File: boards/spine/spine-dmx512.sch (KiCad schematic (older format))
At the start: 22 parts, among them P2 XLR_3, Q1 IRFML8244, Q2 IRFML8244, U3 NC7WZ14, U4 NC7WZ14, U5 NC7WZ14, U6 SN75176B, X1 100BASET_XFMR

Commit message: Tidy
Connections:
- wire segments 110 -> 106
- no-connect marks 5 -> 9
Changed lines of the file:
@@
 Text Label 1950 1950 0    60   ~ 0
 DMX_TX_OOK
-Text Label 8900 4500 0    60   ~ 0
+Text Label 8950 4500 0    60   ~ 0
 DMX_PWR1
-Text Label 8900 4900 0    60   ~ 0
+Text Label 8950 4900 0    60   ~ 0
 DMX_PWR2
-Text Label 8900 5500 0    60   ~ 0
+Text Label 8950 5500 0    60   ~ 0
 DMX_TX_OOK
-Text Label 8900 5900 0    60   ~ 0
+Text Label 8950 5900 0    60   ~ 0
 DMX_GND
 Text Notes 900  1350 0    60   ~ 0
@@
 Connection ~ 2950 1350
 Wire Wire Line
-	8700 4900 9550 4900
+	8700 4900 9600 4900
 Wire Wire Line
 	2600 1950 1950 1950
@@
 	2600 1050 1950 1050
 Wire Wire Line
-	8700 4500 9550 4500
-Wire Wire Line
-	8700 5500 9550 5500
-Wire Wire Line
-	8700 4700 8800 4700
-Wire Wire Line
-	8700 5900 8800 5900
-Wire Wire Line
-	8800 5900 9550 5900
-Connection ~ 8800 5900
-Wire Wire Line
-	8800 4700 8800 5900
+	8700 4500 9600 4500
+Wire Wire Line
+	8700 5500 9600 5500
+Wire Wire Line
+	8700 4700 8850 4700
+Wire Wire Line
+	8700 5900 8850 5900
+Wire Wire Line
+	8850 5900 9600 5900
+Connection ~ 8850 5900
+Wire Wire Line
+	8850 4700 8850 5900
 Wire Wire Line
 	5500 5900 6950 5900
@@
 	2600 6350 3850 6350
 Wire Wire Line
-	4200 6350 4800 6350
-Wire Wire Line
-	4800 6350 5400 6350
-Wire Wire Line
-	5400 6350 5950 6350
+	3850 6350 4800 6350
+Wire Wire Line
+	4800 6350 5950 6350
 Wire Wire Line
 	5950 6350 6400 6350
@@
 	3150 4050 3850 4050
 Wire Wire Line
-	3850 4050 4200 4050
-Wire Wire Line
-	4200 4050 4800 4050
-Wire Wire Line
-	4800 4050 5400 4050
-Wire Wire Line
-	5400 4050 6800 4050
+	3850 4050 4800 4050
+Wire Wire Line
+	4800 4050 6800 4050
 Connection ~ 6800 4700
 Wire Wire Line
@@
 Connection ~ 3850 4050
 Wire Wire Line
-	3850 4900 3850 6350
+	3850 6350 3850 4900
 Connection ~ 2850 4050
 Connection ~ 3850 6350
@@
 Text Notes 6900 6200 0    60   ~ 0
 DC blocking
-Wire Wire Line
-	3850 6350 4200 6350
+NoConn ~ 4050 4950
+NoConn ~ 4050 5350
+NoConn ~ 5000 5700
+NoConn ~ 5000 6100
 $EndSCHEMATC

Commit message: Get the BOM started
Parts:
- removed unit 1 of U4
- added unit 1 of U5
- C1, C2, C7: value .1uF -> 0.1uF; MfgId (none) -> CC0805ZRY5V9BB104; MfrId (none) -> Yageo; RefPrice1k (none) -> 0.00783; Vend1 (none) -> Digikey; Vend1Id (none) -> 311-1361-1-ND
- C3, C6: MfgId (none) -> CC0805ZKY5V6BB106; MfrId CC0805ZKY5V6BB106 -> Yageo; RefPrice1k (none) -> 0.03080; Vend1 (none) -> Digikey; Vend1Id (none) -> 311-1355-1-ND
- C4, C5: MfgId (none) -> CC0805KRX7R9BB102; MfrId (none) -> Yageo; RefPrice1k (none) -> 0.00981; Vend1 (none) -> Digikey; Vend1Id (none) -> 311-1127-1-ND
- D1, D2: value D_Schottky_x2_KCom_AAK -> BAT54 2x common cathode; MfrId (none) -> Diodes Inc; RefPrice1k (none) -> .03955; Vend1 (none) -> Digikey; Vend1Id (none) -> BAT54C-FDICT-ND
- D3: value 20V -> TVS 20V Zener; MfgId (none) -> MMBZ20VALT1G; MfrId MMBZ20VALT1G -> ON Semi; RefPrice1k (none) -> .04208; Vend1 (none) -> Digikey; Vend1Id (none) -> MMBZ20VALT1GOSCT-ND
- P2: value XLR_3 -> XLR-3 Female; MfgId (none) -> NC3FAAH2-0; MfrId (none) -> Neutrik; RefPrice1k (none) -> 0.653; Vend1 (none) -> Mouser; Vend1Id (none) -> 568-NC3FAAH-2-O
- Q1, Q2: MfgId (none) -> IRFML8244TRPBF; MfrId (none) -> Infineon; RefPrice1k (none) -> 0.1046; Vend1 (none) -> Digikey; Vend1Id (none) -> IRFML8244TRPBFCT-ND
- R1, R2: MfgId (none) -> RMCF0805JT4K70; MfrId (none) -> Stackpole; RefPrice1k (none) -> 0.0032; Vend1 (none) -> Digikey; Vend1Id (none) -> RMCF0805JT4K70CT-ND
- R3: MfgId (none) -> RMCF0805JT150R; MfrId (none) -> Stackpole; RefPrice1k (none) -> 0.0032; Vend1 (none) -> Digikey; Vend1Id (none) -> RMCF0805JT150RCT-ND
- R4: MfgId (none) -> RMCF0805JT1M00; MfrId (none) -> Stackpole; RefPrice1k (none) -> 0.0032; Vend1 (none) -> Digikey; Vend1Id (none) -> RMCF0805JT1M00CT-ND
- T1: renamed from X1; value 100BASET_XFMR -> 10/100baseT transformer; footprint xess-J00-0045 -> (none); MfgId (none) -> PT61018PEL; MfrId (none) -> Bourns; RefPrice1k (none) -> 0.78; Vend1 (none) -> Mouser; Vend1Id (none) -> 652-PT61018PEL
- U3, U4, U5: MfgId (none) -> NC7WZ14P6X; MfrId (none) -> Fairchild; RefPrice1k (none) -> 0.07631; Vend1 (none) -> Digikey; Vend1Id (none) -> NC7WZ14P6XCT-ND
- U4: renamed from U5; MfgId (none) -> NC7WZ14P6X; MfrId (none) -> Fairchild; RefPrice1k (none) -> 0.07631; Vend1 (none) -> Digikey; Vend1Id (none) -> NC7WZ14P6XCT-ND
- U6: MfgId (none) -> SN75176BDR; MfrId (none) -> Texas Instruments; RefPrice1k (none) -> 0.330; Vend1 (none) -> Digikey; Vend1Id (none) -> 296-1275-1-ND
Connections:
- wire segments 106 -> 81

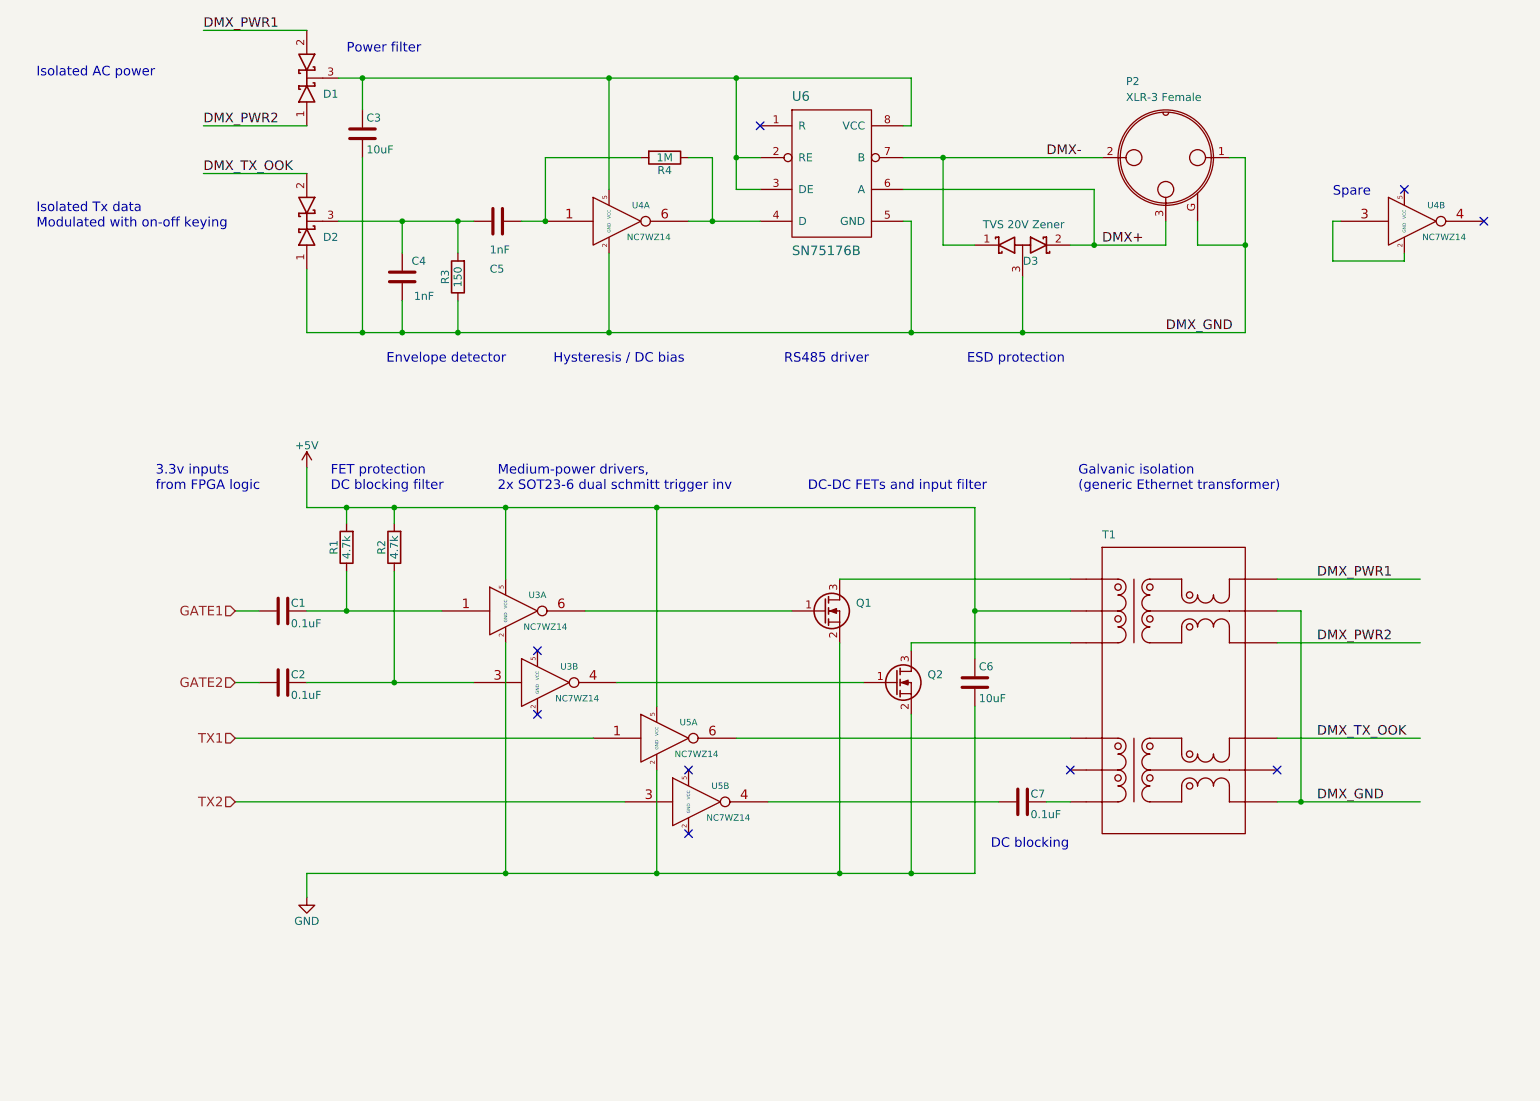
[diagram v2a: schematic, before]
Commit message: USB port: ESD, crystal, eeprom
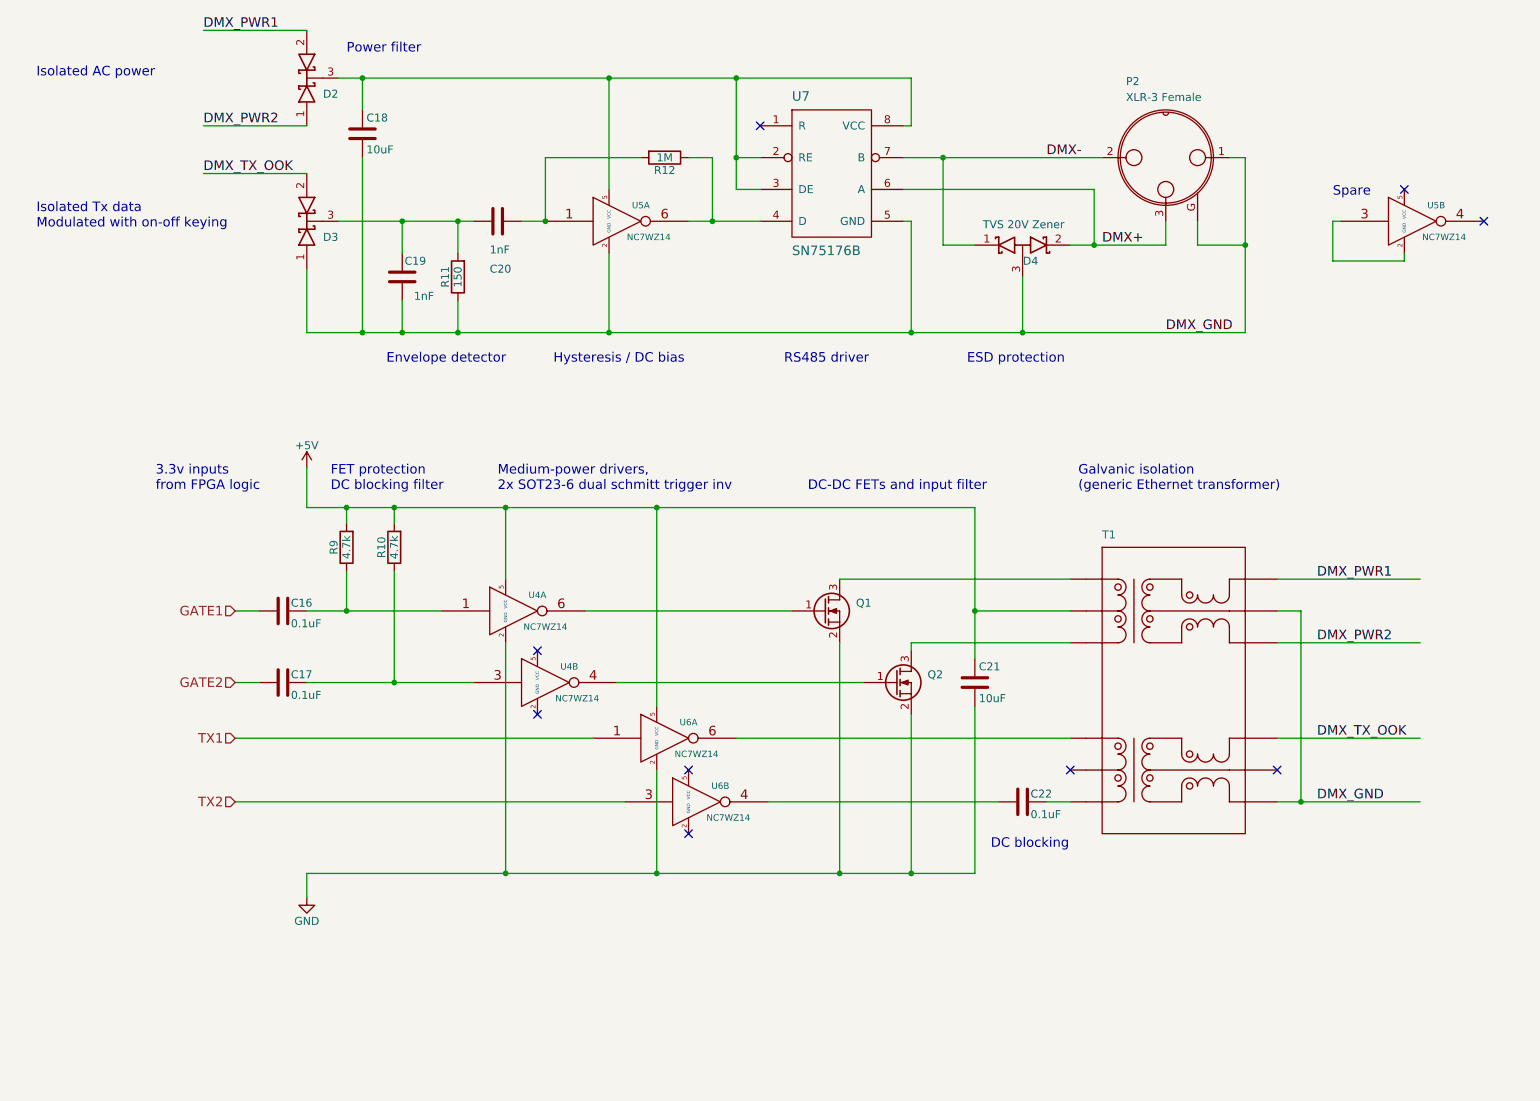
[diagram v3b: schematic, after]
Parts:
- renumbered C1 to C16, C2 to C17, C3 to C18, C4 to C19, C5 to C20, C6 to C21, C7 to C22, D1 to D2, D2 to D3, D3 to D4, R2 to R10, R3 to R11, R4 to R12, R1 to R9, U3 to U4, U4 to U5, U5 to U6, U6 to U7
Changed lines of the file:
@@
 DMX-
 $Comp
-L SN75176B U6
+L SN75176B U7
 U 1 1 563E894A
 P 5950 1550
-F 0 "U6" H 5650 1600 60  0000 L BNN
+F 0 "U7" H 5650 1600 60  0000 L BNN
 F 1 "SN75176B" H 5650 700 60  0000 L TNN
 F 2 "" H 5950 1550 60  0000 C CNN
@@
 $EndComp
 $Comp
-L D_Schottky_x2_ACom_KKA D3
+L D_Schottky_x2_ACom_KKA D4
 U 1 1 563E8FC2
 P 7100 2400
-F 0 "D3" H 7150 2300 50  0000 C CNN
+F 0 "D4" H 7150 2300 50  0000 C CNN
 F 1 "TVS 20V Zener" H 6850 2500 50  0000 L BNN
 F 2 "" H 7100 2400 60  0000 C CNN
@@
 $EndComp
 $Comp
-L NC7WZ14 U4
+L NC7WZ14 U5
 U 1 1 563ECD2E
 P 4550 2250
-F 0 "U4" H 4700 2350 40  0000 C CNN
+F 0 "U5" H 4700 2350 40  0000 C CNN
 F 1 "NC7WZ14" H 4750 2150 40  0000 C CNN
 F 2 "" H 4550 2250 60  0000 C CNN
@@
 NoConn ~ 9500 2050
 $Comp
-L R R4
+L R R12
 U 1 1 563ED073
 P 4850 1850
-F 0 "R4" V 4930 1850 50  0000 C CNN
+F 0 "R12" V 4930 1850 50  0000 C CNN
 F 1 "1M" V 4850 1850 50  0000 C CNN
 F 2 "" V 4780 1850 30  0000 C CNN
@@
 NoConn ~ 10000 2250
 $Comp
-L C C4
+L C C19
 U 1 1 563EDC1A
 P 3200 2600
-F 0 "C4" H 3050 2700 50  0000 L CNN
+F 0 "C19" H 3050 2700 50  0000 L CNN
 F 1 "1nF" H 3000 2450 50  0000 L BNN
 F 2 "" H 3238 2450 30  0000 C CNN
@@
 $EndComp
 $Comp
-L D_Schottky_x2_KCom_AAK D2
+L D_Schottky_x2_KCom_AAK D3
 U 1 1 563EE535
 P 2600 2250
-F 0 "D2" V 2500 2100 50  0000 C CNN
+F 0 "D3" V 2500 2100 50  0000 C CNN
 F 1 "BAT54 2x common cathode" H 2600 2350 50  0001 C CNN
 F 2 "" H 2600 2250 60  0000 C CNN
@@
 NoConn ~ 7400 5700
 $Comp
-L C C6
+L C C21
 U 1 1 563F0E74
 P 6800 5150
-F 0 "C6" H 6825 5250 50  0000 L CNN
+F 0 "C21" H 6825 5250 50  0000 L CNN
 F 1 "10uF " H 6825 5050 50  0000 L CNN
 F 2 "" H 6838 5000 30  0000 C CNN
@@
 $EndComp
 $Comp
-L GND #PWR02
+L GND #PWR18
 U 1 1 563F2AEF
 P 2600 6500
-F 0 "#PWR02" H 2600 6250 50  0001 C CNN
+F 0 "#PWR18" H 2600 6250 50  0001 C CNN
 F 1 "GND" H 2600 6350 50  0000 C CNN
 F 2 "" H 2600 6500 60  0000 C CNN
@@
 $EndComp
 $Comp
-L C C1
+L C C16
 U 1 1 563F4706
 P 2450 4700
-F 0 "C1" V 2400 4750 50  0000 L CNN
+F 0 "C16" V 2400 4750 50  0000 L CNN
 F 1 "0.1uF" V 2500 4750 50  0000 L TNN
 F 2 "" H 2488 4550 30  0000 C CNN
@@
 $EndComp
 $Comp
-L +5V #PWR03
+L +5V #PWR17
 U 1 1 563F515D
 P 2600 3800
-F 0 "#PWR03" H 2600 3650 50  0001 C CNN
+F 0 "#PWR17" H 2600 3650 50  0001 C CNN
 F 1 "+5V" H 2600 3940 50  0000 C CNN
 F 2 "" H 2600 3800 60  0000 C CNN
@@
 NoConn ~ 5000 6100
 $Comp
-L D_Schottky_x2_KCom_AAK D1
+L D_Schottky_x2_KCom_AAK D2
 U 1 1 563ED560
 P 2600 1350
-F 0 "D1" V 2500 1200 50  0000 C CNN
+F 0 "D2" V 2500 1200 50  0000 C CNN
 F 1 "BAT54 2x common cathode" H 2600 1450 50  0001 C CNN
 F 2 "" H 2600 1350 60  0000 C CNN
@@
 $EndComp
 $Comp
-L C C3
+L C C18
 U 1 1 563F1736
 P 2950 1700
-F 0 "C3" H 2975 1800 50  0000 L CNN
+F 0 "C18" H 2975 1800 50  0000 L CNN
 F 1 "10uF " H 2975 1600 50  0000 L CNN
 F 2 "" H 2988 1550 30  0000 C CNN
@@
 $EndComp
 $Comp
-L NC7WZ14 U4
+L NC7WZ14 U5
 U 2 1 563F235B
 P 9550 2250
-F 0 "U4" H 9700 2350 40  0000 C CNN
+F 0 "U5" H 9700 2350 40  0000 C CNN
 F 1 "NC7WZ14" H 9750 2150 40  0000 C CNN
 F 2 "" H 9550 2250 60  0000 C CNN
@@
 $EndComp
 $Comp
-L NC7WZ14 U3
+L NC7WZ14 U4
 U 1 1 563F23E5
 P 3900 4700
-F 0 "U3" H 4050 4800 40  0000 C CNN
+F 0 "U4" H 4050 4800 40  0000 C CNN
 F 1 "NC7WZ14" H 4100 4600 40  0000 C CNN
 F 2 "" H 3900 4700 60  0000 C CNN
@@
 $EndComp
 $Comp
-L NC7WZ14 U3
+L NC7WZ14 U4
 U 2 1 563F2462
 P 4100 5150
-F 0 "U3" H 4250 5250 40  0000 C CNN
+F 0 "U4" H 4250 5250 40  0000 C CNN
 F 1 "NC7WZ14" H 4300 5050 40  0000 C CNN
 F 2 "" H 4100 5150 60  0000 C CNN
@@
 $EndComp
 $Comp
-L NC7WZ14 U5
+L NC7WZ14 U6
 U 1 1 563F2A79
 P 4850 5500
-F 0 "U5" H 5000 5600 40  0000 C CNN
+F 0 "U6" H 5000 5600 40  0000 C CNN
 F 1 "NC7WZ14" H 5050 5400 40  0000 C CNN
 F 2 "" H 4850 5500 60  0000 C CNN
@@
 $EndComp
 $Comp
-L NC7WZ14 U5
+L NC7WZ14 U6
 U 2 1 563F2AF3
 P 5050 5900
-F 0 "U5" H 5200 6000 40  0000 C CNN
+F 0 "U6" H 5200 6000 40  0000 C CNN
 F 1 "NC7WZ14" H 5250 5800 40  0000 C CNN
 F 2 "" H 5050 5900 60  0000 C CNN
@@
 $EndComp
 $Comp
-L R R3
+L R R11
 U 1 1 563F3452
 P 3550 2600
-F 0 "R3" V 3630 2600 50  0000 C CNN
+F 0 "R11" V 3630 2600 50  0000 C CNN
 F 1 "150" V 3550 2600 50  0000 C CNN
 F 2 "" V 3480 2600 30  0000 C CNN
@@
 $EndComp
 $Comp
-L R R1
+L R R9
 U 1 1 563F362A
 P 2850 4300
-F 0 "R1" V 2930 4300 50  0000 C CNN
+F 0 "R9" V 2930 4300 50  0000 C CNN
 F 1 "4.7k" V 2850 4300 50  0000 C CNN
 F 2 "" V 2780 4300 30  0000 C CNN
@@
 $EndComp
 $Comp
-L R R2
+L R R10
 U 1 1 563F3881
 P 3150 4300
-F 0 "R2" V 3230 4300 50  0000 C CNN
+F 0 "R10" V 3230 4300 50  0000 C CNN
 F 1 "4.7k" V 3150 4300 50  0000 C CNN
 F 2 "" V 3080 4300 30  0000 C CNN
@@
 $EndComp
 $Comp
-L C C2
+L C C17
 U 1 1 563F48B8
 P 2450 5150
-F 0 "C2" V 2400 5200 50  0000 L CNN
+F 0 "C17" V 2400 5200 50  0000 L CNN
 F 1 "0.1uF" V 2500 5200 50  0000 L TNN
 F 2 "" H 2488 5000 30  0000 C CNN
@@
 $EndComp
 $Comp
-L C C7
+L C C22
 U 1 1 563F4920
 P 7100 5900
-F 0 "C7" V 7050 5950 50  0000 L CNN
+F 0 "C22" V 7050 5950 50  0000 L CNN
 F 1 "0.1uF" V 7150 5950 50  0000 L TNN
 F 2 "" H 7138 5750 30  0000 C CNN
@@
 $EndComp
 $Comp
-L C C5
+L C C20
 U 1 1 563F55AB
 P 3800 2250
-F 0 "C5" V 3500 2200 50  0000 L CNN
+F 0 "C20" V 3500 2200 50  0000 L CNN
 F 1 "1nF" V 3650 2200 50  0000 L BNN
 F 2 "" H 3838 2100 30  0000 C CNN

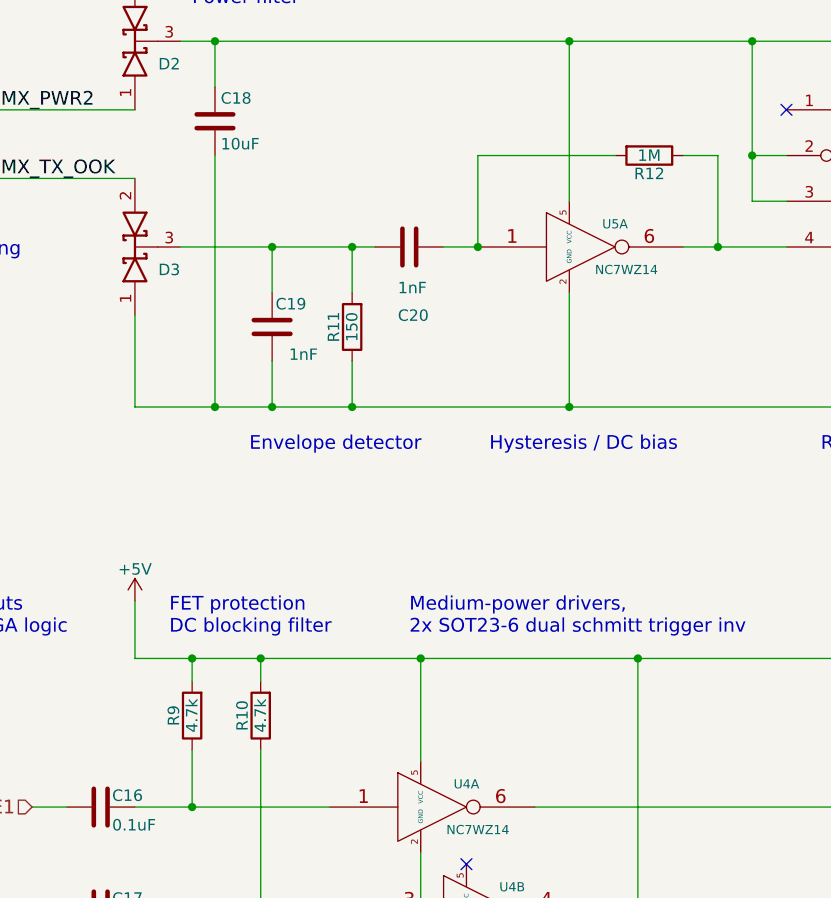
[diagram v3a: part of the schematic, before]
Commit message: More schematic work: module ports and USB
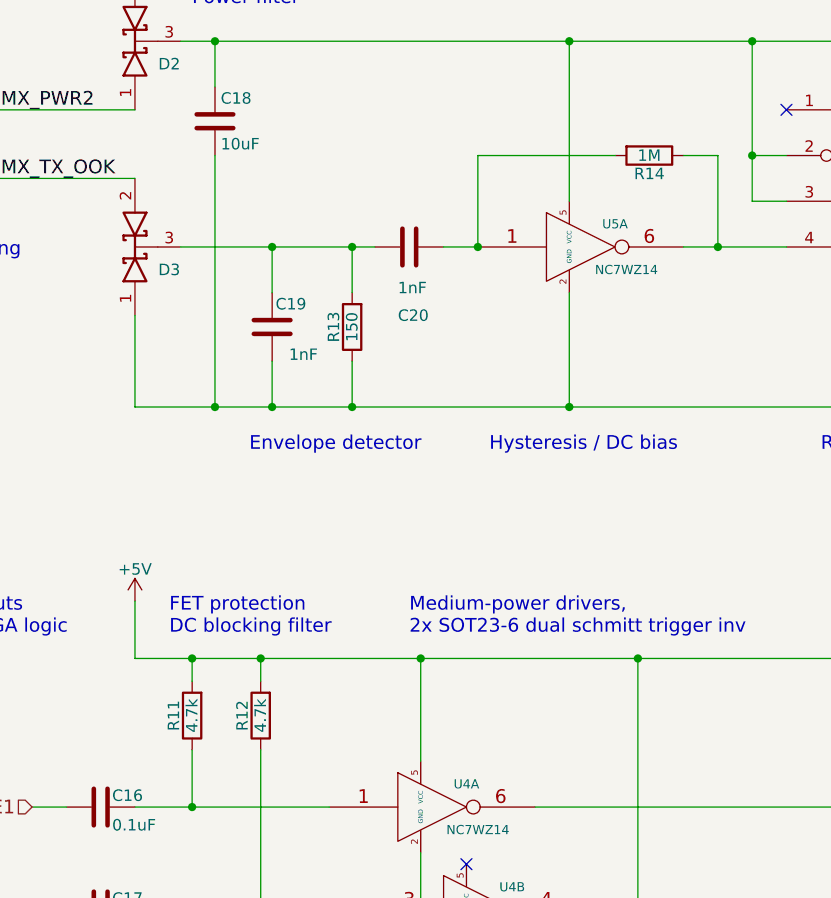
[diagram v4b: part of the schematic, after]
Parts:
- renumbered R9 to R11, R10 to R12, R11 to R13, R12 to R14
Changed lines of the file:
@@
 $Descr USLetter 11000 8500
 encoding utf-8
-Sheet 4 4
+Sheet 4 5
 Title ""
 Date ""
@@
 NoConn ~ 9500 2050
 $Comp
-L R R12
+L R R14
 U 1 1 563ED073
 P 4850 1850
-F 0 "R12" V 4930 1850 50  0000 C CNN
+F 0 "R14" V 4930 1850 50  0000 C CNN
 F 1 "1M" V 4850 1850 50  0000 C CNN
 F 2 "" V 4780 1850 30  0000 C CNN
@@
 $EndComp
 $Comp
-L GND #PWR18
+L GND #PWR017
 U 1 1 563F2AEF
 P 2600 6500
-F 0 "#PWR18" H 2600 6250 50  0001 C CNN
+F 0 "#PWR017" H 2600 6250 50  0001 C CNN
 F 1 "GND" H 2600 6350 50  0000 C CNN
 F 2 "" H 2600 6500 60  0000 C CNN
@@
 $EndComp
 $Comp
-L +5V #PWR17
+L +5V #PWR018
 U 1 1 563F515D
 P 2600 3800
-F 0 "#PWR17" H 2600 3650 50  0001 C CNN
+F 0 "#PWR018" H 2600 3650 50  0001 C CNN
 F 1 "+5V" H 2600 3940 50  0000 C CNN
 F 2 "" H 2600 3800 60  0000 C CNN
@@
 $EndComp
 $Comp
-L R R11
+L R R13
 U 1 1 563F3452
 P 3550 2600
-F 0 "R11" V 3630 2600 50  0000 C CNN
+F 0 "R13" V 3630 2600 50  0000 C CNN
 F 1 "150" V 3550 2600 50  0000 C CNN
 F 2 "" V 3480 2600 30  0000 C CNN
@@
 $EndComp
 $Comp
-L R R9
+L R R11
 U 1 1 563F362A
 P 2850 4300
-F 0 "R9" V 2930 4300 50  0000 C CNN
+F 0 "R11" V 2930 4300 50  0000 C CNN
 F 1 "4.7k" V 2850 4300 50  0000 C CNN
 F 2 "" V 2780 4300 30  0000 C CNN
@@
 $EndComp
 $Comp
-L R R10
+L R R12
 U 1 1 563F3881
 P 3150 4300
-F 0 "R10" V 3230 4300 50  0000 C CNN
+F 0 "R12" V 3230 4300 50  0000 C CNN
 F 1 "4.7k" V 3150 4300 50  0000 C CNN
 F 2 "" V 3080 4300 30  0000 C CNN
